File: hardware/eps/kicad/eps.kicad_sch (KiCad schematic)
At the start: 17 parts, among them J5 XT30PW-F, J9 68000-102HLF

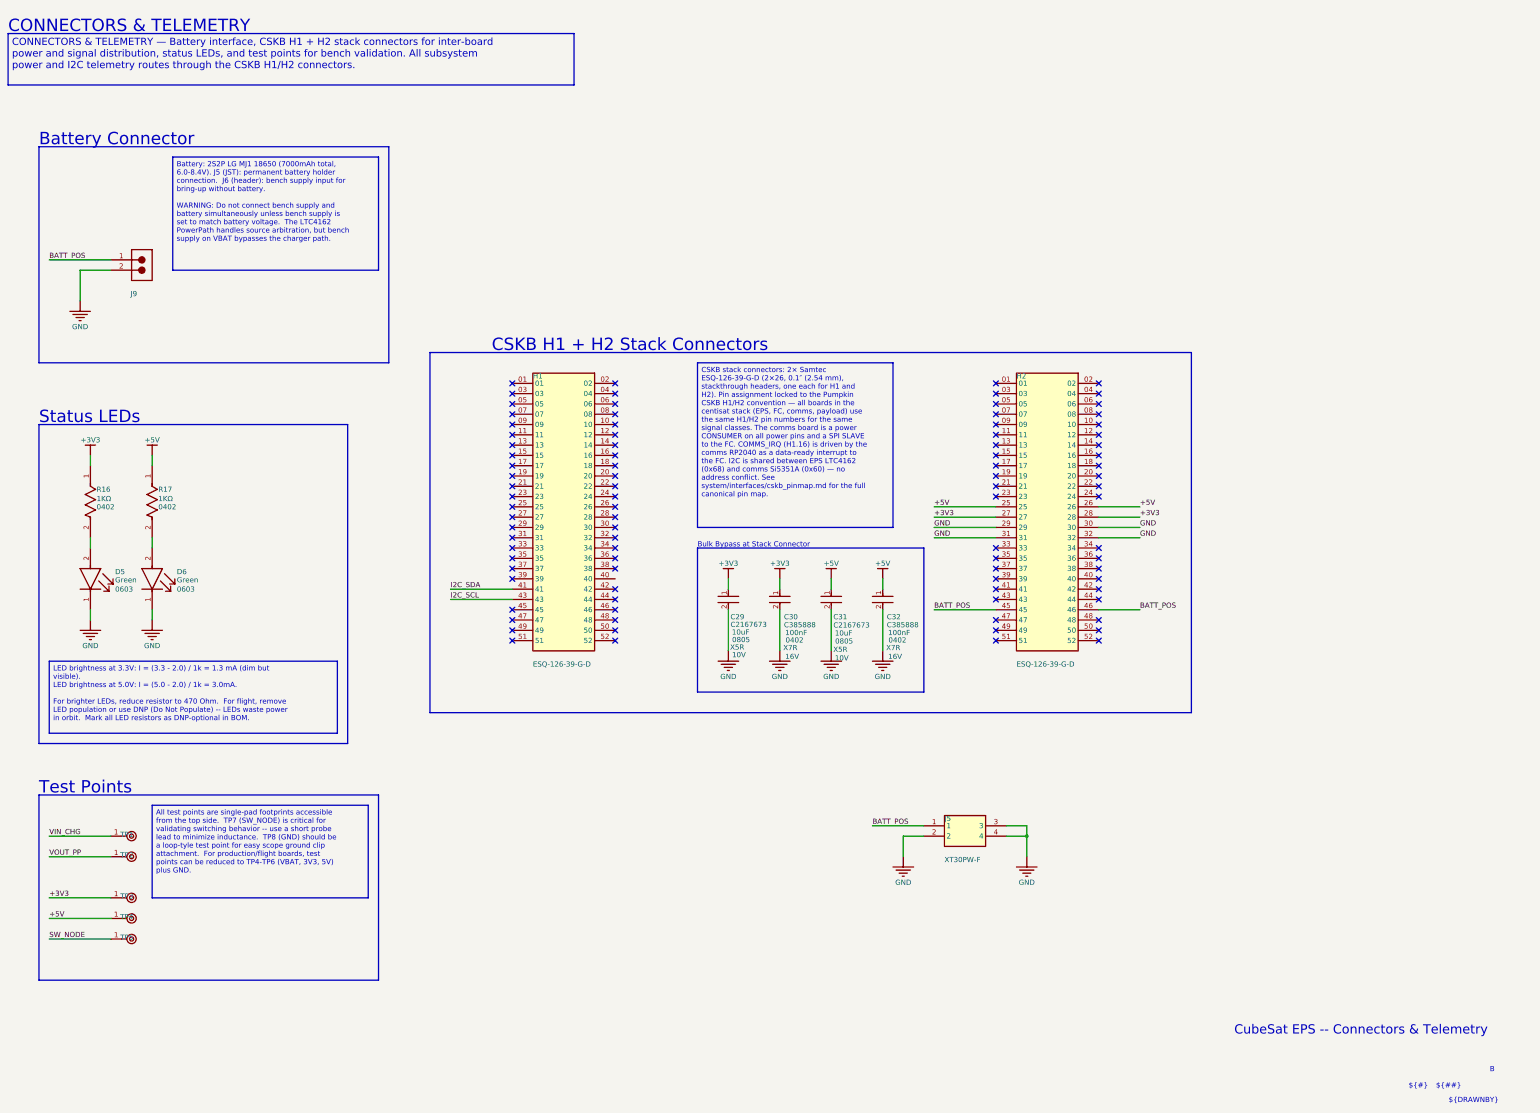
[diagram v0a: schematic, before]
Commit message: attempt to convert altium to kicad, lost foot prints, not good
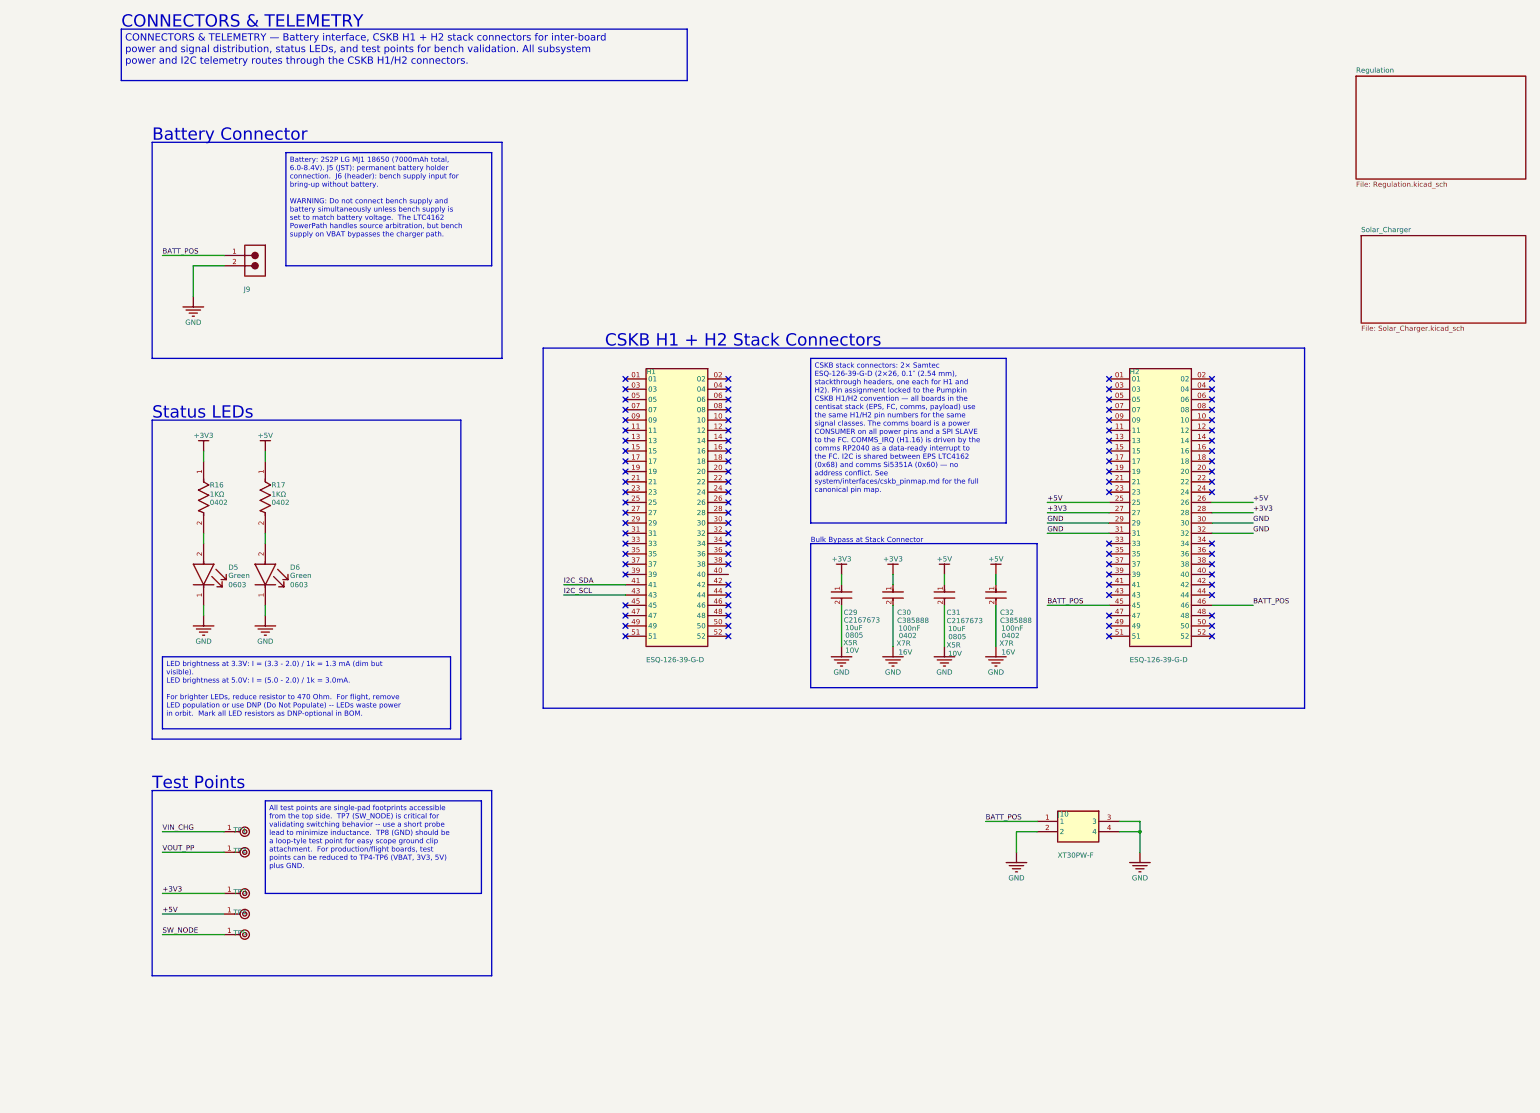
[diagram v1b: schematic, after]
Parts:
- renumbered J5 to J10
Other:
- added sheet Regulation (Regulation.kicad_sch)
- added sheet Solar_Charger (Solar_Charger.kicad_sch)
- note removed: "${##}"
- note removed: "${#}"
- note removed: "${DRAWNBY}"
- note removed: "${REVISION}"
- note removed: "${TITLE}"
- moved on the sheet: C29, C30, C31, C32, D5, D6, H1, H2, J10, J9, R16, R17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

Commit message: eps/kicad: assemble the schematic hierarchy and link it to the PCB
  The three .kicad_sch files were independent roots from the Altium import.
  Opening the project showed only the root's 17 components; the other 60
  were in files KiCad had no path to. Separately, the PCB shared no UUIDs
  at all with any schematic -- it had been imported independently, so the
  board-to-schematic link did not exist rather than being broken.

  Both are now fixed. Root sheet carries sheet symbols for Regulation and
  Solar_Charger, and all 77 footprints link to their symbols: 17 on the
  root, 28 in Regulation, 32 in Solar_Charger, matching the schematics
  exactly. Sheet-local nets picked up hierarchical paths, which cleared
  the "via connected to unknown net" warnings.

  Getting there took several passes and two things had to be repaired
  first.

  Annotation. Building the hierarchy in KiCad re-annotated the child
  sheets -- Solar_Charger went J1-J8 to J11-J18, C1-C24 became C41-C52 --
  because a duplicate J5 blocked the assembly. The refdes are the only
  link to the board, so 69 footprints were deleted as orphans. Every
  symbol UUID survived, so the old annotation was restored exactly by
  UUID, and the board was restored from the previous commit. The J5
  collision is resolved properly: J5 is the JST connector, and the XT30
  that shared its designator is now J10, on both the schematic and the
  board.

  Footprint fields. The import left them unusable -- only 5 of 40 carried
  a library prefix, and 10 pointed at
  C__Users_dng_Documents_AltiumLL_SamacSys.PcbLib, a Windows path from the
  machine that ran the import. All 77 are now the board's own qualified
  ids, which removed about 60 "missing a library name" warnings per
  update.

  The last 11 footprints would not link no matter how the update dialog
  was configured: KiCad matched 66 by UUID path and never fell back to
  reference designators for the remainder. Their paths were written
  directly instead, following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
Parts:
- C29, C31: footprint FP-C0805C-DG-MFG -> Vault:FP-C0805C-DG-MFG
- C30, C32: footprint FP-0402-L_1_0_0_05-W_0_5-MFG -> Vault:FP-0402-L_1_0_0_05-W_0_5-MFG
- D5, D6: footprint FP-LTST-S270KGKT-MFG -> Vault:FP-LTST-S270KGKT-MFG
- H1, H2: footprint SAMTEC_ESQ-126-39-G-D -> Vault:SAMTEC_ESQ-126-39-G-D
- J10: footprint XT30PWF -> Vault:XT30PWF
- J9: footprint AMPH-68000-102HLF_V -> Vault:AMPH-68000-102HLF_V
- R16, R17: footprint FP-CRGCQ0402-IPC_C -> Vault:FP-CRGCQ0402-IPC_C
- TP1, TP2, TP3, TP4, TP5: footprint TP06R -> Vault:TP06R
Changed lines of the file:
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@@
 			)
 		)
-		(property "Footprint" "AMPH-68000-102HLF_V"
+		(property "Footprint" "Vault:AMPH-68000-102HLF_V"
 			(at 66.04 80.01 0)
 			(hide yes)
@@
 			)
 		)
-		(property "Footprint" "TP06R"
+		(property "Footprint" "Vault:TP06R"
 			(at 60.96 250.19 0)
 			(hide yes)
@@
 			)
 		)
-		(property "Footprint" "FP-LTST-S270KGKT-MFG"
+		(property "Footprint" "Vault:FP-LTST-S270KGKT-MFG"
 			(at 55.88 153.67 0)
 			(hide yes)
@@
 			)
 		)
-		(property "Footprint" "TP06R"
+		(property "Footprint" "Vault:TP06R"
 			(at 60.96 229.87 0)
 			(hide yes)
@@
 			)
 		)
-		(property "Footprint" "FP-0402-L_1_0_0_05-W_0_5-MFG"
+		(property "Footprint" "Vault:FP-0402-L_1_0_0_05-W_0_5-MFG"
 			(at 251.46 163.83 0)
 			(hide yes)
@@
 			)
 		)
-		(property "Footprint" "TP06R"
+		(property "Footprint" "Vault:TP06R"
 			(at 60.96 240.03 0)
 			(hide yes)
@@
 			)
 		)
-		(property "Footprint" "TP06R"
+		(property "Footprint" "Vault:TP06R"
 			(at 60.96 245.11 0)
 			(hide yes)
@@
 			)
 		)
-		(property "Footprint" "FP-CRGCQ0402-IPC_C"
+		(property "Footprint" "Vault:FP-CRGCQ0402-IPC_C"
 			(at 55.88 133.35 0)
 			(hide yes)
@@
 			)
 		)
-		(property "Footprint" "FP-CRGCQ0402-IPC_C"
+		(property "Footprint" "Vault:FP-CRGCQ0402-IPC_C"
 			(at 71.12 133.35 0)
 			(hide yes)
@@
 			)
 		)
-		(property "Footprint" "FP-LTST-S270KGKT-MFG"
+		(property "Footprint" "Vault:FP-LTST-S270KGKT-MFG"
 			(at 71.12 153.67 0)
 			(hide yes)
@@
 			)
 		)
-		(property "Footprint" "SAMTEC_ESQ-126-39-G-D"
+		(property "Footprint" "Vault:SAMTEC_ESQ-126-39-G-D"
 			(at 172.72 146.05 0)
 			(hide yes)
@@
 			)
 		)
-		(property "Footprint" "SAMTEC_ESQ-126-39-G-D"
+		(property "Footprint" "Vault:SAMTEC_ESQ-126-39-G-D"
 			(at 292.1 146.05 0)
 			(hide yes)
@@
 			)
 		)
-		(property "Footprint" "FP-C0805C-DG-MFG"
+		(property "Footprint" "Vault:FP-C0805C-DG-MFG"
 			(at 213.36 163.83 0)
 			(hide yes)
@@
 			)
 		)
-		(property "Footprint" "XT30PWF"
+		(property "Footprint" "Vault:XT30PWF"
 			(at 261.62 222.25 0)
 			(hide yes)
@@
 			)
 		)
-		(property "Footprint" "TP06R"
+		(property "Footprint" "Vault:TP06R"
 			(at 60.96 224.79 0)
 			(hide yes)
@@
 			)
 		)
-		(property "Footprint" "FP-C0805C-DG-MFG"
+		(property "Footprint" "Vault:FP-C0805C-DG-MFG"
 			(at 238.76 163.83 0)
 			(hide yes)
@@
 			)
 		)
-		(property "Footprint" "FP-0402-L_1_0_0_05-W_0_5-MFG"
+		(property "Footprint" "Vault:FP-0402-L_1_0_0_05-W_0_5-MFG"
 			(at 226.06 163.83 0)
 			(hide yes)
